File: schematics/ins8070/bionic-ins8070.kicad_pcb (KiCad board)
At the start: 2 copper layers, 27.9 x 68.6 mm, 8 parts, among them J1 Bionic-P135, J2 Bionic-P245, U1 INS8070, U2 11AA010-I/TT

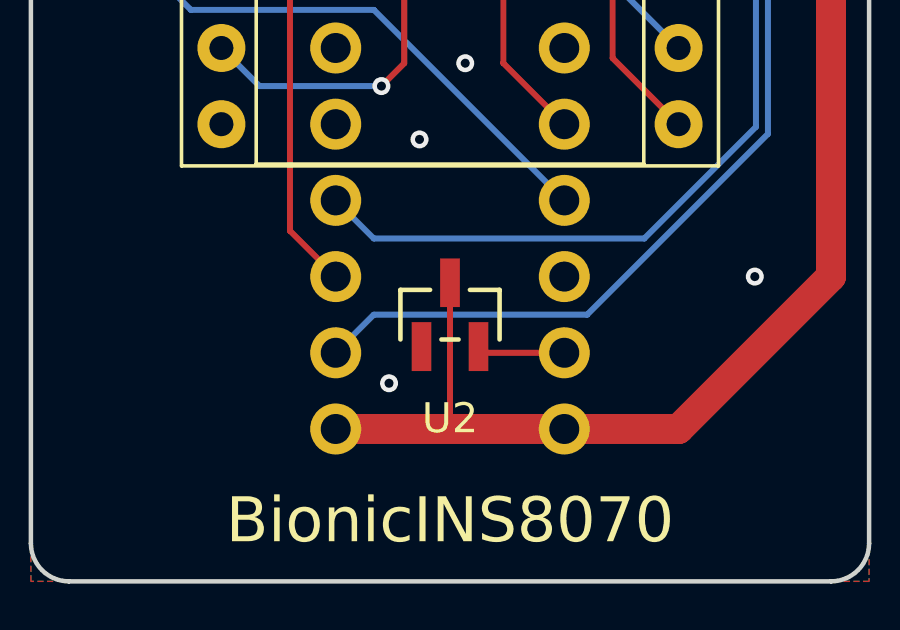
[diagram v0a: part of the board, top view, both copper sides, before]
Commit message: [INS8070] Fix EEPROM pinout
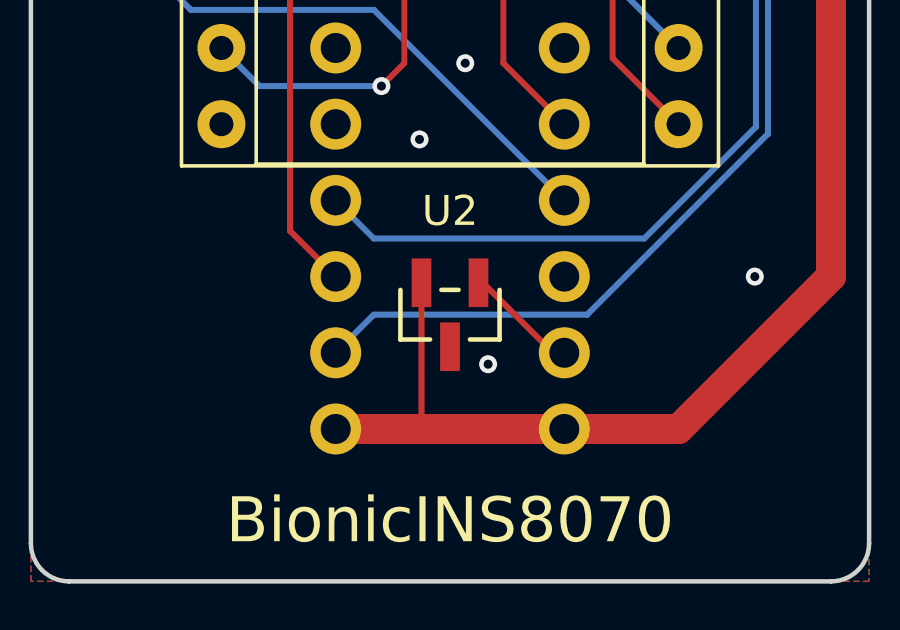
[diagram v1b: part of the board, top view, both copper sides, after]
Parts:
- turned U2 to 180 degrees
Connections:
- U2 pad 1: GND -> Net-(J2-P57)
- U2 pad 2: Net-(J2-P57) -> VCC
- U2 pad 3: VCC -> GND
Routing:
- net Net-(J2-P57): track 2.94 -> 3.83 mm
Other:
- board text added: "Rev. 5"
- board text removed: "Rev. 4"
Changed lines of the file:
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@@
   (title_block
     (title "BionicINS8070")
-    (date "2024-04-24")
-    (rev "3")
+    (date "2024-11-01")
+    (rev "5")
     (company "Tadashi G. Takaoka")
   )
@@
   )
   (footprint "0-LocalLibrary:SOT-23_MC_MCH-M" (layer "F.Cu")
-    (at 114.97 129.69)
+    (at 114.97 129.69 180)
     (descr "Microchip 11AAxxx-I/TT UNI/O 1Kbit Serial EEPROM")
     (property "Sheetfile" "bionic-ins8070.kicad_sch")
@@
         (effects (font (size 1 1) (thickness 0.15)))
     )
-    (fp_text value "11AA010-I/TT" (at 0 0 unlocked) (layer "F.Fab")
+    (fp_text value "11AA010-I/TT" (at 0 0 180 unlocked) (layer "F.Fab")
         (effects (font (size 1 1) (thickness 0.15)))
     )
-    (fp_text user "${REFERENCE}" (at 0 0 unlocked) (layer "F.Fab")
+    (fp_text user "${REFERENCE}" (at 0 0 180 unlocked) (layer "F.Fab")
         (effects (font (size 1 1) (thickness 0.15)))
     )
@@
     (fp_circle (center -1.270999 0.446) (end -1.143999 0.446)
       (stroke (width 0.0254) (type solid)) (fill none) (layer "F.Fab"))
-    (pad "1" smd rect (at -0.950001 1.066) (size 0.6604 1.6256) (layers "F.Cu" "F.Paste" "F.Mask")
+    (pad "1" smd rect (at -0.950001 1.066 180) (size 0.6604 1.6256) (layers "F.Cu" "F.Paste" "F.Mask")
+      (net 10 "Net-(J2-P57)") (pinfunction "SCIO") (pintype "bidirectional"))
+    (pad "2" smd rect (at 0.950001 1.066 180) (size 0.6604 1.6256) (layers "F.Cu" "F.Paste" "F.Mask")
+      (net 1 "VCC") (pinfunction "VCC") (pintype "power_in"))
+    (pad "3" smd rect (at 0 -1.066 180) (size 0.6604 1.6256) (layers "F.Cu" "F.Paste" "F.Mask")
       (net 2 "GND") (pinfunction "VSS") (pintype "power_in"))
-    (pad "2" smd rect (at 0.950001 1.066) (size 0.6604 1.6256) (layers "F.Cu" "F.Paste" "F.Mask")
-      (net 10 "Net-(J2-P57)") (pinfunction "SCIO") (pintype "bidirectional"))
-    (pad "3" smd rect (at 0 -1.066) (size 0.6604 1.6256) (layers "F.Cu" "F.Paste" "F.Mask")
-      (net 1 "VCC") (pinfunction "VCC") (pintype "power_in"))
     (model "${KIPRJMOD}/0-LocalLibrary/SOT-23_MC_MCH.step"
       (offset (xyz 0 0 0))
@@
     (effects (font (size 0.8 0.8)) (justify bottom mirror))
   )
-  (gr_text "Rev. 4" (at 107.096 136.802) (layer "B.SilkS")
+  (gr_text "Rev. 5" (at 107.096 136.802) (layer "B.SilkS")
     (effects (font (size 1 1)) (justify left mirror))
   )
@@
   (segment (start 127.67 77.62) (end 127.67 75.535) (width 1) (layer "F.Cu") (net 1))
   (segment locked (start 122.59 133.5) (end 127.67 128.42) (width 1) (layer "F.Cu") (net 1))
+  (segment (start 113.954 133.5) (end 118.78 133.5) (width 1) (layer "F.Cu") (net 1))
   (segment locked (start 125.13 75.08) (end 122.59 75.08) (width 1) (layer "F.Cu") (net 1))
+  (segment (start 111.16 133.5) (end 113.954 133.5) (width 1) (layer "F.Cu") (net 1))
+  (segment (start 114.019999 128.624) (end 114.019999 133.434001) (width 0.2) (layer "F.Cu") (net 1))
+  (segment (start 114.019999 133.434001) (end 113.954 133.5) (width 0.2) (layer "F.Cu") (net 1))
   (segment (start 127.215 75.08) (end 125.13 75.08) (width 1) (layer "F.Cu") (net 1))
   (segment (start 127.67 75.535) (end 127.215 75.08) (width 1) (layer "F.Cu") (net 1))
-  (segment (start 114.97 133.5) (end 114.97 128.624) (width 0.2) (layer "F.Cu") (net 1))
-  (segment locked (start 111.16 133.5) (end 118.78 133.5) (width 1) (layer "F.Cu") (net 1))
   (via (at 125.13 128.42) (size 0.6) (drill 0.3) (layers "F.Cu" "B.Cu") (net 2))
   (via (at 115.478 121.308) (size 0.6) (drill 0.3) (layers "F.Cu" "B.Cu") (free) (net 2))
   (via (at 113.954 123.848) (size 0.6) (drill 0.3) (layers "F.Cu" "B.Cu") (free) (net 2))
   (via (at 126.273 76.858) (size 0.6) (drill 0.3) (layers "F.Cu" "B.Cu") (net 2))
-  (via (at 112.938 131.976) (size 0.6) (drill 0.3) (layers "F.Cu" "B.Cu") (net 2))
+  (via (at 116.24 131.341) (size 0.6) (drill 0.3) (layers "F.Cu" "B.Cu") (free) (net 2))
   (segment (start 125.568 123.664) (end 125.568 85.678) (width 0.2) (layer "B.Cu") (net 3))
   (segment (start 111.16 130.96) (end 112.43 129.69) (width 0.2) (layer "B.Cu") (net 3))
@@
   (segment (start 114.062 101.223) (end 112.049 99.21) (width 0.2) (layer "B.Cu") (net 9))
   (segment (start 114.062 103.89) (end 114.062 101.223) (width 0.2) (layer "B.Cu") (net 9))
-  (segment (start 118.78 130.96) (end 116.124 130.96) (width 0.2) (layer "F.Cu") (net 10))
-  (segment (start 116.124 130.96) (end 115.92 130.756) (width 0.2) (layer "F.Cu") (net 10))
+  (segment (start 116.063 128.624) (end 118.399 130.96) (width 0.2) (layer "F.Cu") (net 10))
+  (segment (start 115.920001 128.624) (end 116.063 128.624) (width 0.2) (layer "F.Cu") (net 10))
+  (segment (start 118.399 130.96) (end 118.78 130.96) (width 0.2) (layer "F.Cu") (net 10))
   (segment (start 114.624714 88.288) (end 113.446 89.466714) (width 0.2) (layer "F.Cu") (net 12))
   (segment (start 113.446 89.466714) (end 113.446 121.308) (width 0.2) (layer "F.Cu") (net 12))

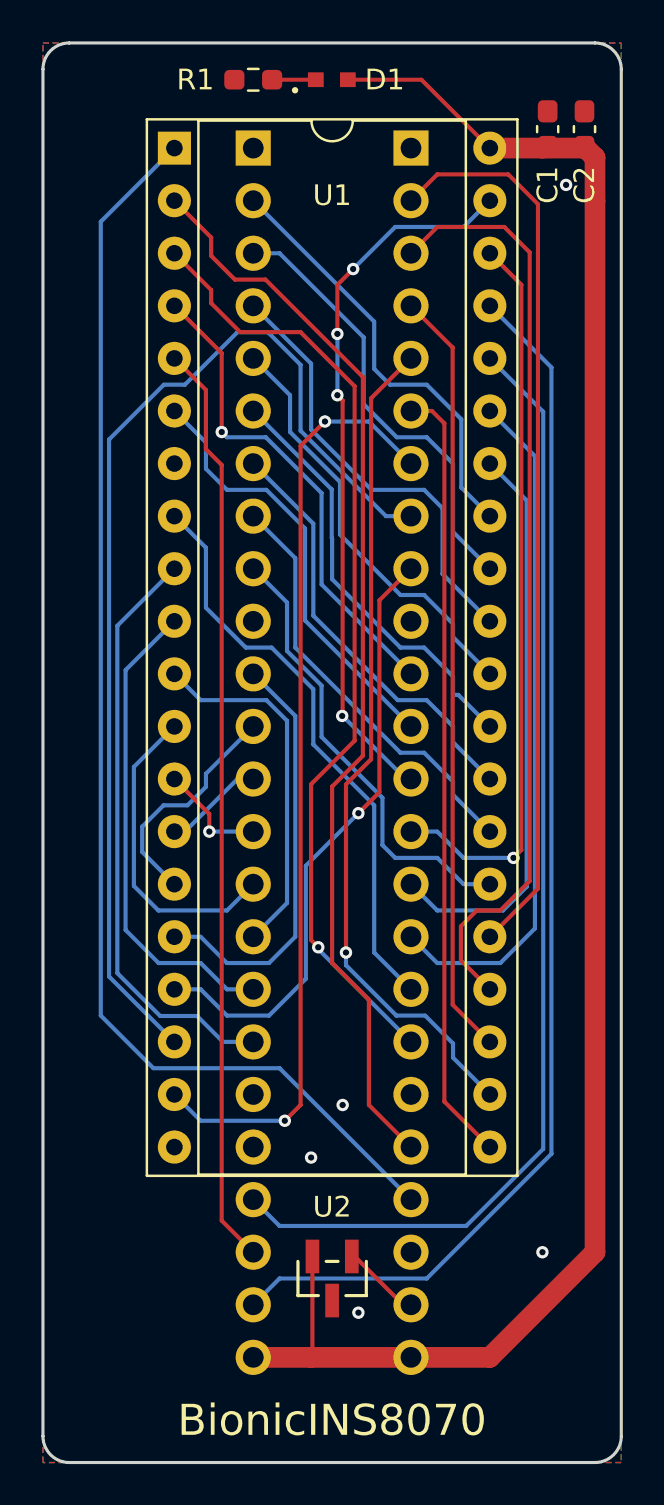
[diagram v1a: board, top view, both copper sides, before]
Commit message: [INS8070] Shrink board size
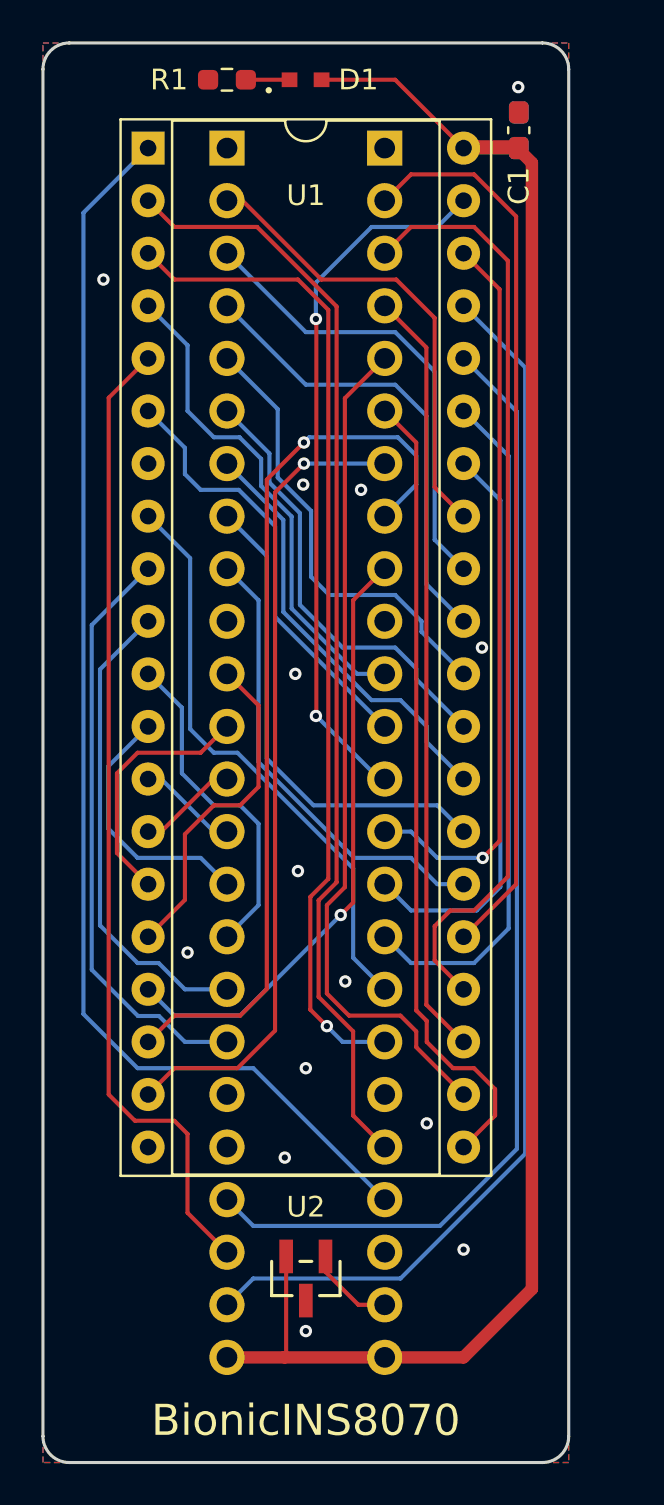
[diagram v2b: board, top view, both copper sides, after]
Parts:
- C2: moved to B.Cu
- moved C2 3.18 mm to (124.0, 74.2)
- moved C1 1.40 mm to (124.0, 74.2)
- moved D1 1.27 mm to (113.7, 71.8)
- moved J1 1.27 mm to (109.9, 75.1)
- moved J2 1.27 mm to (117.5, 75.1)
- moved R1 1.27 mm to (109.9, 71.8)
- moved U1 1.27 mm to (106.1, 75.1)
- moved U2 1.27 mm to (113.7, 129.7)
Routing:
- net /P26: track 52.7 -> 43.4 mm, vias 0 -> 1
- net /P25: track 45.4 -> 39.3 mm, vias 2 -> 1
- net /P30: track 20.4 -> 16.3 mm
- net /P16: track 20.6 -> 23.5 mm
- net /P34: track 15.3 -> 12.6 mm
- net /P52: track 44.8 -> 47.5 mm
- net VCC: track 90.2 -> 92.5 mm
- net /P47: track 46.3 -> 48.2 mm
- net /P10: track 21.0 -> 22.5 mm
- net /P24: track 37.7 -> 39.0 mm
- net /P35: track 17.5 -> 16.3 mm
- net /P13: track 20.6 -> 21.8 mm
- net /P31: track 11.2 -> 12.2 mm
- net /P12: track 21.5 -> 22.5 mm
- net /P54: track 52.6 -> 53.5 mm
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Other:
- board size 27.9 x 68.6 mm -> 25.4 x 68.6 mm

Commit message: [INS8070] Fix SA/SB connections
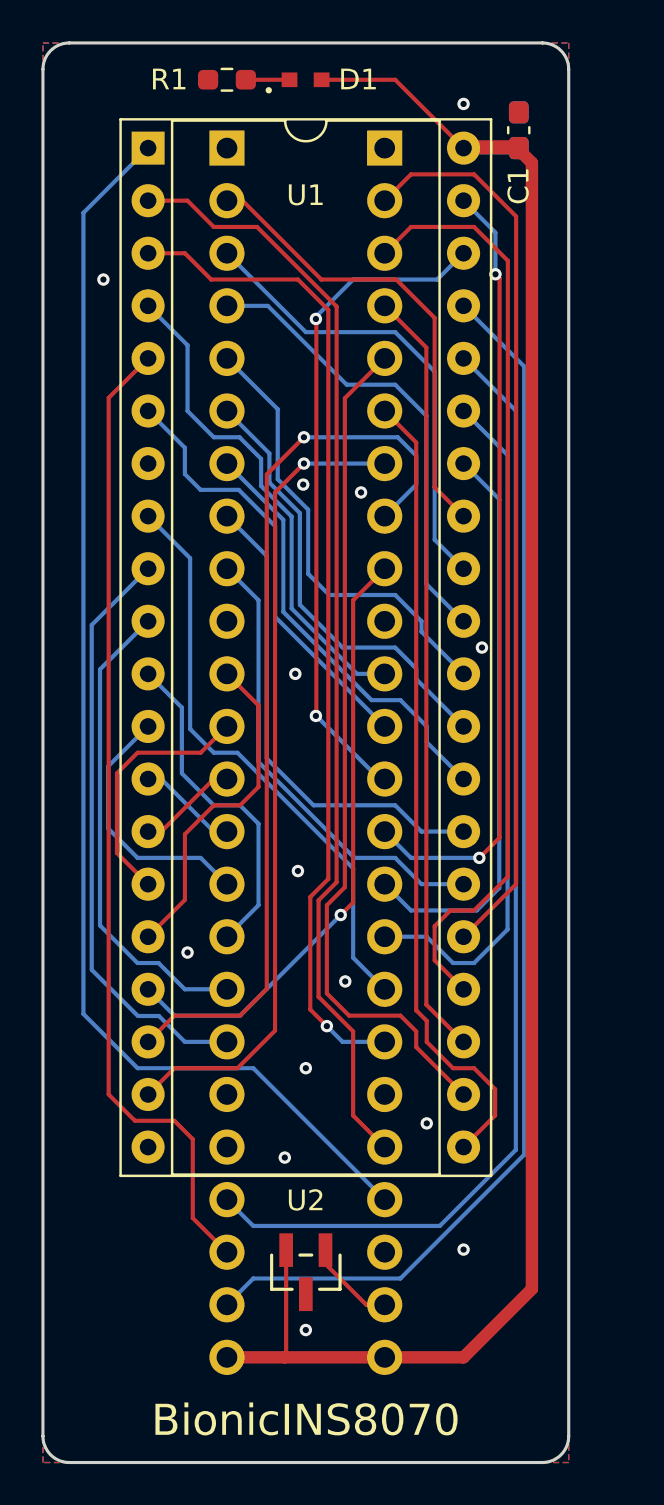
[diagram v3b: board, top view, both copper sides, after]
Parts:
- moved U2 0.31 mm to (113.7, 129.4)
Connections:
- U1 pad 38: /P43 -> /P42
- U1 pad 39: /P42 -> /P43
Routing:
- net /P43: track 35.5 -> 38.0 mm, vias 1 -> 2
- net /P42: track 34.3 -> 32.3 mm
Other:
- board text added: "Rev. 6"
- board text removed: "Rev. 5"

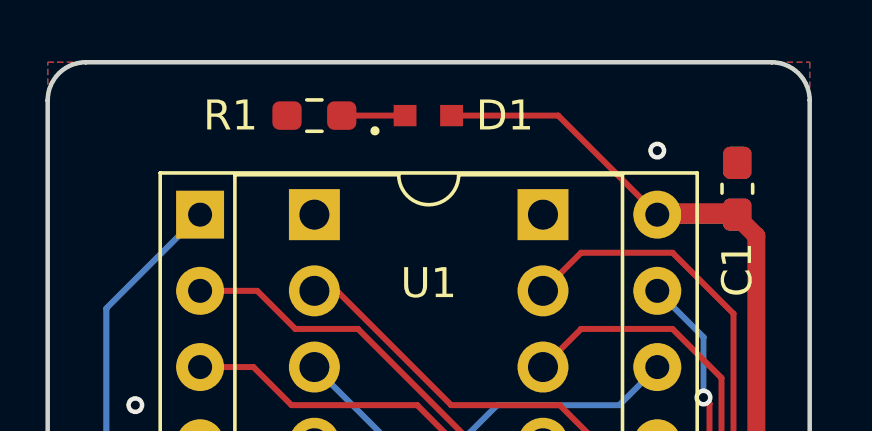
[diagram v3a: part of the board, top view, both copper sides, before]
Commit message: [schematics] Update LED footprint
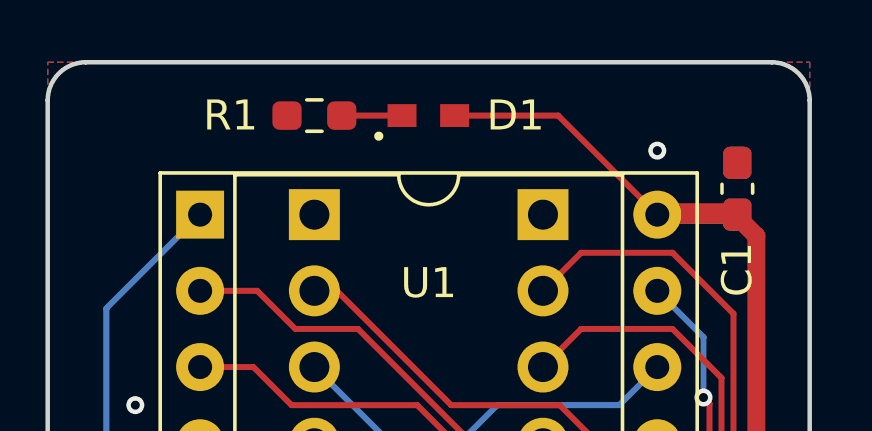
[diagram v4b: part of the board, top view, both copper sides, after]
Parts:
- D1: footprint 0-LocalLibrary:LED_CSL1901UW1_ROM -> 0-LocalLibrary:LED_CSL1901UW1_ROM-M

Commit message: [INS8070] Cleanup schematics
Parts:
- D1: footprint 0-LocalLibrary:LED_CSL1901UW1_ROM-M -> rhom:LED_CSL1901UW1_ROM-M
- J1: footprint 0-LocalLibrary:Bionic-P135_Vertical -> bionic:Bionic-P135_Vertical
- J2: footprint 0-LocalLibrary:Bionic-P245_Vertical -> bionic:Bionic-P245_Vertical
- U1: footprint 0-LocalLibrary:DIP-40_W15.24mm_Socket -> bionic:DIP-40_W15.24mm_Socket
- U2: footprint 0-LocalLibrary:SOT-23_MC_MCH-M -> microchip:SOT-23_MC_MCH-M
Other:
- rule pad_to_mask_clearance: 0.051 -> 0

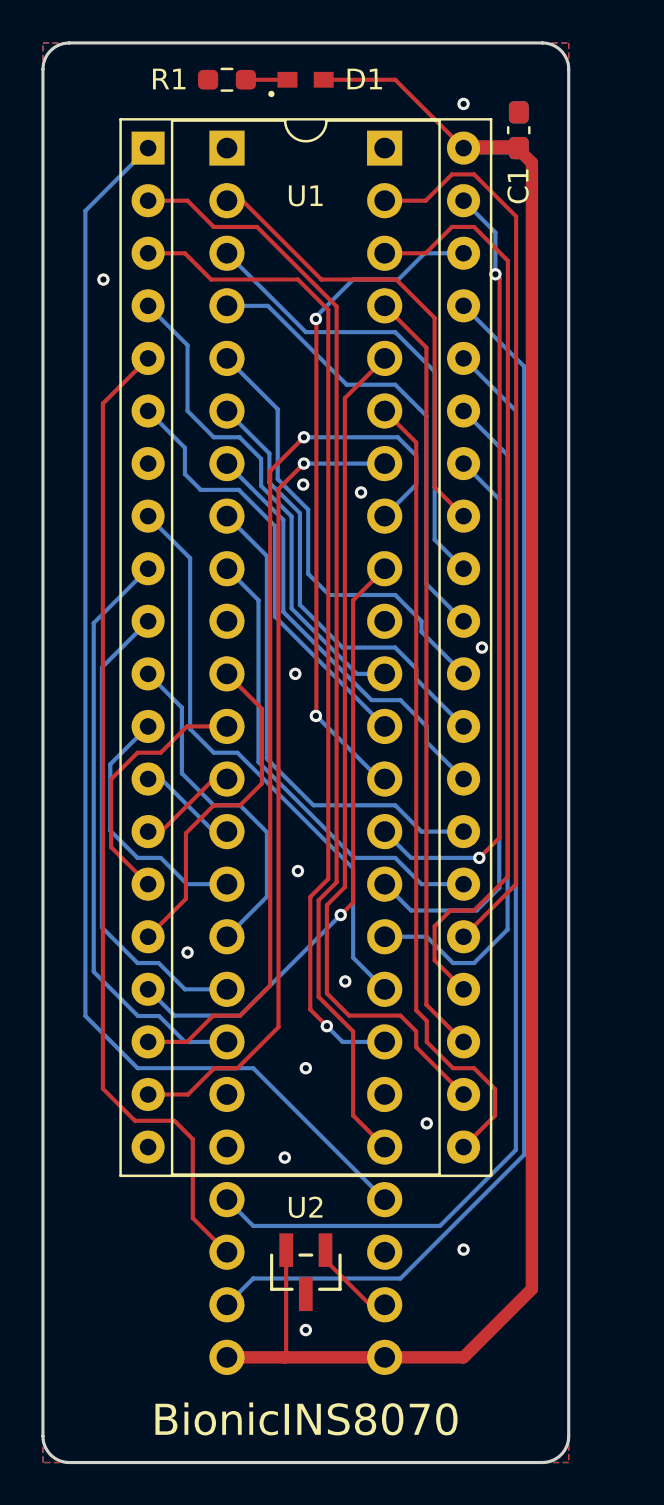
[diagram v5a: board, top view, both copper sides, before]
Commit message: [INS8070] Update schematics
Remove unused pins from bionic connector
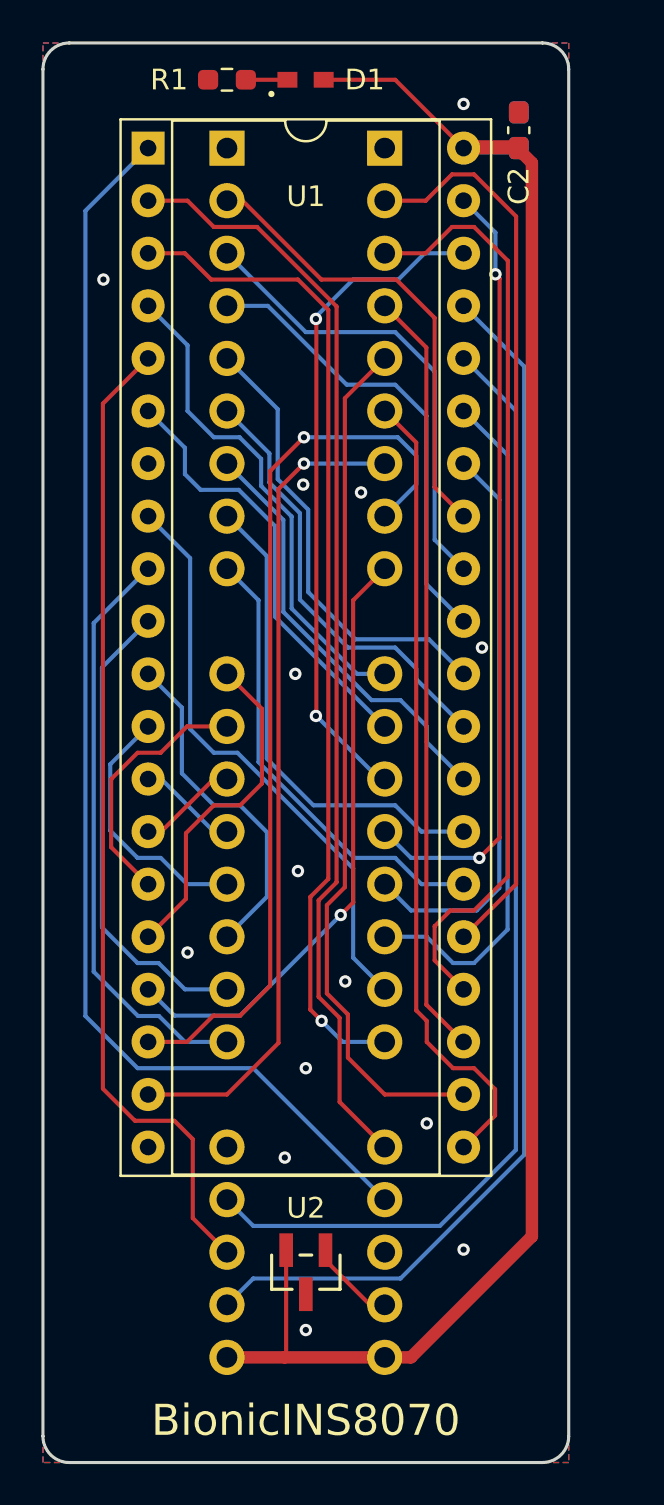
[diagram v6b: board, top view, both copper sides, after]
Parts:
- C1: moved to B.Cu
- C2: moved to F.Cu
- J1: footprint bionic:Bionic-P135_Vertical -> bionic:Bionic-P135_THT
- J2: footprint bionic:Bionic-P245_Vertical -> bionic:Bionic-P245_THT
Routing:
- net VCC: track 92.8 -> 91.3 mm
- net /P23: track 40.9 -> 41.7 mm
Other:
- board text added: "Rev. 7"
- board text removed: "Rev. 6"
